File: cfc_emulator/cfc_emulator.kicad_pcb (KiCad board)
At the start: 2 copper layers, 51.3 x 51.1 mm, 23 parts, among them J1 pirt_test_conn, J2 PMOD1A, J3 PMOD1B, U1 DS90CR217MTD_NOPBMTD48_TEX-L

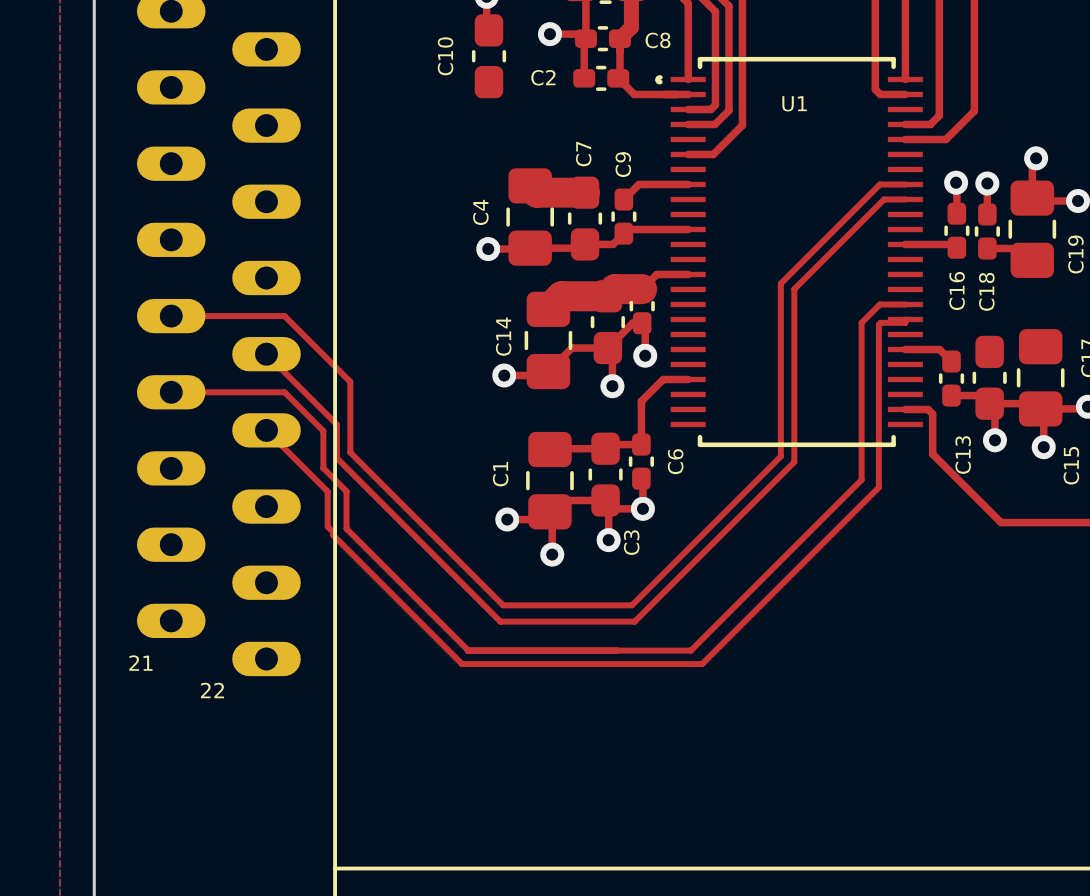
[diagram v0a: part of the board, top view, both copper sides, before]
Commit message: Tweak up diff pairs and remove gerbers
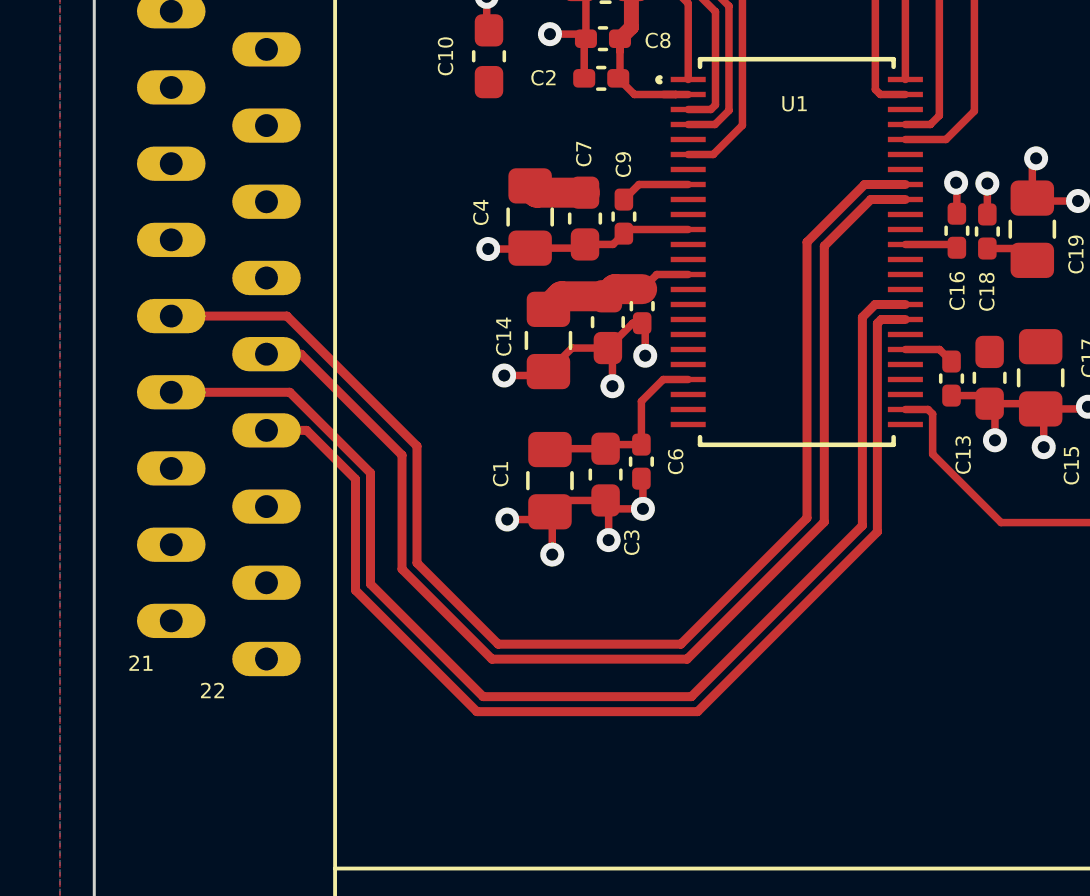
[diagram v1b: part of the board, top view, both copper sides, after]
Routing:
- net /LVDS0+: track 34.8 -> 39.5 mm
- net /LVDS0-: track 39.0 -> 43.0 mm
- net /LVDSCLK+: track 33.3 -> 36.8 mm
- net /LVDSCLK-: track 42.4 -> 40.3 mm
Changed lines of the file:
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@@
   (segment (start 163.137028 89.028528) (end 161.529613 89.028528) (width 0.25) (layer "F.Cu") (net 15))
   (segment (start 153.878528 84.028528) (end 153.456413 84.028528) (width 0.25) (layer "F.Cu") (net 15))
-  (segment (start 143.0274 95.9612) (end 148.122615 101.056415) (width 0.2) (layer "F.Cu") (net 21))
-  (segment (start 148.122615 101.056415) (end 152.415215 101.056415) (width 0.2) (layer "F.Cu") (net 21))
-  (segment (start 152.415215 101.056415) (end 157.3784 96.09323) (width 0.2) (layer "F.Cu") (net 21))
-  (segment (start 140.837418 91.4146) (end 143.0274 93.604582) (width 0.2) (layer "F.Cu") (net 21))
-  (segment (start 137.0584 91.4146) (end 140.837418 91.4146) (width 0.2) (layer "F.Cu") (net 21))
-  (segment (start 157.3784 96.09323) (end 157.3784 90.331817) (width 0.2) (layer "F.Cu") (net 21))
-  (segment (start 157.3784 90.331817) (end 160.681689 87.028528) (width 0.2) (layer "F.Cu") (net 21))
-  (segment (start 143.0274 93.604582) (end 143.0274 95.9612) (width 0.2) (layer "F.Cu") (net 21))
-  (segment (start 160.681689 87.028528) (end 161.529613 87.028528) (width 0.2) (layer "F.Cu") (net 21))
-  (segment (start 142.57789 95.02909) (end 142.57789 96.147394) (width 0.2) (layer "F.Cu") (net 22))
-  (segment (start 160.817393 87.528528) (end 161.529613 87.528528) (width 0.2) (layer "F.Cu") (net 22))
-  (segment (start 157.827911 96.279423) (end 157.827911 90.51801) (width 0.2) (layer "F.Cu") (net 22))
-  (segment (start 142.57789 96.147394) (end 148.030496 101.6) (width 0.2) (layer "F.Cu") (net 22))
-  (segment (start 140.2334 92.6846) (end 142.57789 95.02909) (width 0.2) (layer "F.Cu") (net 22))
-  (segment (start 152.507334 101.6) (end 157.827911 96.279423) (width 0.2) (layer "F.Cu") (net 22))
-  (segment (start 148.030496 101.6) (end 152.507334 101.6) (width 0.2) (layer "F.Cu") (net 22))
-  (segment (start 157.827911 90.51801) (end 160.817393 87.528528) (width 0.2) (layer "F.Cu") (net 22))
-  (segment (start 154.381364 102.565036) (end 160.0708 96.8756) (width 0.2) (layer "F.Cu") (net 23))
-  (segment (start 140.837418 93.9546) (end 142.128379 95.245561) (width 0.2) (layer "F.Cu") (net 23))
-  (segment (start 160.0708 96.8756) (end 160.0708 91.639417) (width 0.2) (layer "F.Cu") (net 23))
-  (segment (start 146.938836 102.565036) (end 151.942964 102.565036) (width 0.2) (layer "F.Cu") (net 23))
-  (segment (start 142.128379 96.483861) (end 142.900409 97.255891) (width 0.2) (layer "F.Cu") (net 23))
-  (segment (start 137.0584 93.9546) (end 140.837418 93.9546) (width 0.2) (layer "F.Cu") (net 23))
-  (segment (start 142.900409 97.255891) (end 142.900409 98.501209) (width 0.2) (layer "F.Cu") (net 23))
-  (segment (start 146.938836 102.539636) (end 146.938836 102.565036) (width 0.2) (layer "F.Cu") (net 23))
-  (segment (start 142.128379 95.245561) (end 142.128379 96.483861) (width 0.2) (layer "F.Cu") (net 23))
-  (segment (start 160.681689 91.028528) (end 161.529613 91.028528) (width 0.2) (layer "F.Cu") (net 23))
-  (segment (start 146.938836 102.565036) (end 154.381364 102.565036) (width 0.2) (layer "F.Cu") (net 23))
-  (segment (start 160.0708 91.639417) (end 160.681689 91.028528) (width 0.2) (layer "F.Cu") (net 23))
-  (segment (start 142.900409 98.501209) (end 146.938836 102.539636) (width 0.2) (layer "F.Cu") (net 23))
-  (segment (start 142.450889 98.712793) (end 142.450889 98.611193) (width 0.2) (layer "F.Cu") (net 24))
-  (segment (start 161.529613 91.528528) (end 161.529613 91.640117) (width 0.2) (layer "F.Cu") (net 24))
-  (segment (start 160.645902 91.700019) (end 160.645902 97.124459) (width 0.2) (layer "F.Cu") (net 24))
-  (segment (start 154.755816 103.014545) (end 146.752641 103.014545) (width 0.2) (layer "F.Cu") (net 24))
-  (segment (start 142.450889 98.611193) (end 142.273089 98.433393) (width 0.2) (layer "F.Cu") (net 24))
-  (segment (start 160.645902 97.124459) (end 154.755816 103.014545) (width 0.2) (layer "F.Cu") (net 24))
-  (segment (start 146.752641 103.014545) (end 142.450889 98.712793) (width 0.2) (layer "F.Cu") (net 24))
-  (segment (start 142.273089 98.433393) (end 142.273089 97.264289) (width 0.2) (layer "F.Cu") (net 24))
-  (segment (start 161.529613 91.640117) (end 160.705804 91.640117) (width 0.2) (layer "F.Cu") (net 24))
-  (segment (start 142.273089 97.264289) (end 140.2334 95.2246) (width 0.2) (layer "F.Cu") (net 24))
-  (segment (start 160.705804 91.640117) (end 160.645902 91.700019) (width 0.2) (layer "F.Cu") (net 24))
+  (segment (start 137.0584 91.4146) (end 140.9146 91.4146) (width 0.3) (layer "F.Cu") (net 21))
+  (segment (start 154.045957 102.350489) (end 158.250489 98.145957) (width 0.3) (layer "F.Cu") (net 21))
+  (segment (start 140.9146 91.4146) (end 145.25 95.75) (width 0.3) (layer "F.Cu") (net 21))
+  (segment (start 158.250489 88.949511) (end 160.171472 87.028528) (width 0.3) (layer "F.Cu") (net 21))
+  (segment (start 145.25 99.643584) (end 147.956905 102.350489) (width 0.3) (layer "F.Cu") (net 21))
+  (segment (start 158.250489 98.145957) (end 158.250489 88.949511) (width 0.3) (layer "F.Cu") (net 21))
+  (segment (start 147.956905 102.350489) (end 154.045957 102.350489) (width 0.3) (layer "F.Cu") (net 21))
+  (segment (start 160.171472 87.028528) (end 161.529613 87.028528) (width 0.3) (layer "F.Cu") (net 21))
+  (segment (start 145.25 95.75) (end 145.25 99.643584) (width 0.3) (layer "F.Cu") (net 21))
+  (segment (start 144.750489 99.850489) (end 147.75 102.85) (width 0.3) (layer "F.Cu") (net 22))
+  (segment (start 160.377888 87.528528) (end 161.529613 87.528528) (width 0.3) (layer "F.Cu") (net 22))
+  (segment (start 147.75 102.85) (end 154.253554 102.85) (width 0.3) (layer "F.Cu") (net 22))
+  (segment (start 144.750489 96.050489) (end 144.750489 99.850489) (width 0.3) (layer "F.Cu") (net 22))
+  (segment (start 140.2334 92.6846) (end 141.3846 92.6846) (width 0.3) (layer "F.Cu") (net 22))
+  (segment (start 158.826777 89.079639) (end 160.377888 87.528528) (width 0.3) (layer "F.Cu") (net 22))
+  (segment (start 158.826777 98.276777) (end 158.826777 89.079639) (width 0.3) (layer "F.Cu") (net 22))
+  (segment (start 141.3846 92.6846) (end 144.750489 96.050489) (width 0.3) (layer "F.Cu") (net 22))
+  (segment (start 154.253554 102.85) (end 158.826777 98.276777) (width 0.3) (layer "F.Cu") (net 22))
+  (segment (start 141.011015 93.9546) (end 143.7 96.643585) (width 0.3) (layer "F.Cu") (net 23))
+  (segment (start 160.520299 91.028528) (end 161.529613 91.028528) (width 0.3) (layer "F.Cu") (net 23))
+  (segment (start 143.7 100.346446) (end 147.453554 104.1) (width 0.3) (layer "F.Cu") (net 23))
+  (segment (start 143.7 96.643585) (end 143.7 100.346446) (width 0.3) (layer "F.Cu") (net 23))
+  (segment (start 160.095911 98.400535) (end 160.095911 91.452916) (width 0.3) (layer "F.Cu") (net 23))
+  (segment (start 137.0584 93.9546) (end 141.011015 93.9546) (width 0.3) (layer "F.Cu") (net 23))
+  (segment (start 160.095911 91.452916) (end 160.520299 91.028528) (width 0.3) (layer "F.Cu") (net 23))
+  (segment (start 147.453554 104.1) (end 154.396446 104.1) (width 0.3) (layer "F.Cu") (net 23))
+  (segment (start 154.396446 104.1) (end 160.095911 98.400535) (width 0.3) (layer "F.Cu") (net 23))
+  (segment (start 141.5746 95.2246) (end 143.2 96.85) (width 0.3) (layer "F.Cu") (net 24))
+  (segment (start 154.603554 104.6) (end 160.595902 98.607652) (width 0.3) (layer "F.Cu") (net 24))
+  (segment (start 143.2 96.85) (end 143.2 100.553554) (width 0.3) (layer "F.Cu") (net 24))
+  (segment (start 160.595902 91.660019) (end 160.727393 91.528528) (width 0.3) (layer "F.Cu") (net 24))
+  (segment (start 147.246446 104.6) (end 154.603554 104.6) (width 0.3) (layer "F.Cu") (net 24))
+  (segment (start 160.727393 91.528528) (end 161.529613 91.528528) (width 0.3) (layer "F.Cu") (net 24))
+  (segment (start 160.595902 98.607652) (end 160.595902 91.660019) (width 0.3) (layer "F.Cu") (net 24))
+  (segment (start 140.2334 95.2246) (end 141.5746 95.2246) (width 0.3) (layer "F.Cu") (net 24))
+  (segment (start 143.2 100.553554) (end 147.246446 104.6) (width 0.3) (layer "F.Cu") (net 24))
   (segment (start 170.2816 74.7776) (end 175.26 79.756) (width 0.25) (layer "F.Cu") (net 25))
   (segment (start 170.2816 73.9836) (end 170.2816 74.7776) (width 0.25) (layer "F.Cu") (net 25))

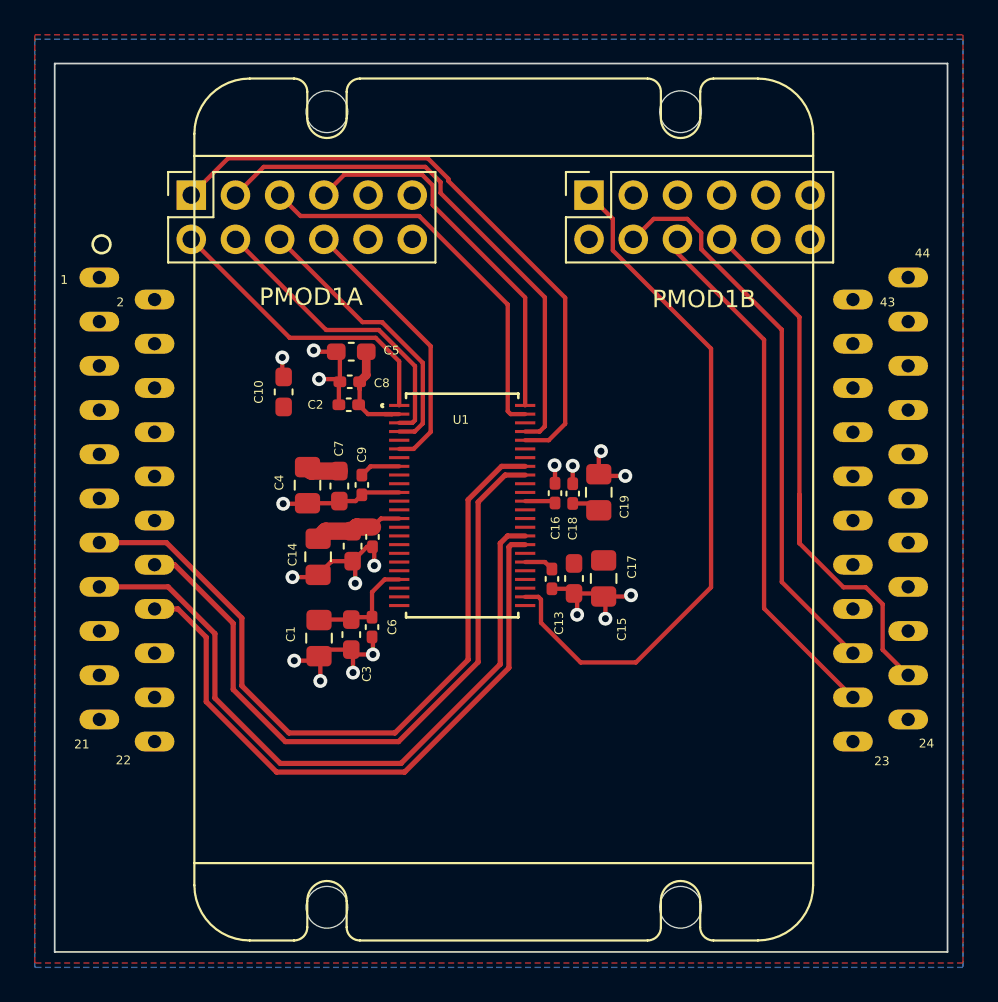
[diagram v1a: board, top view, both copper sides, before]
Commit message: Fix ~powerdown handling to add GPIO control from Icebreaker.  Add pullup on ~powerdown to default it to powered up.  Fix footprint error on TX chip (two pins swapped).  Fix pin swap error on both LVDS pairs.  Add test points to ~powerdown and TXCLK
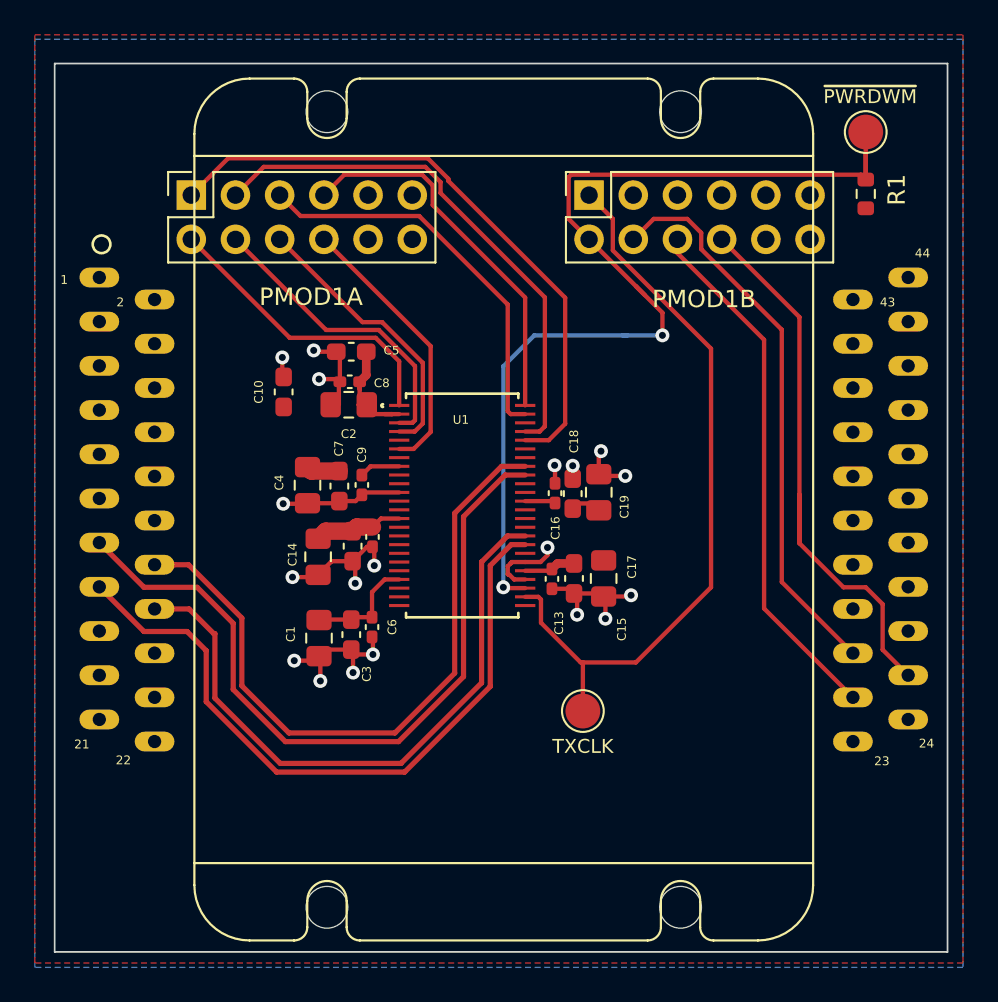
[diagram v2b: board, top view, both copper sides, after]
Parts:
- added R1: 10K, Resistor_SMD:R_0603_1608Metric, F.Cu at (181.1, 71.4)
- added TP1: TXCLK, TestPoint:TestPoint_Pad_D2.0mm, F.Cu at (164.8, 101.1)
- added TP2: ~POWERDOWN, TestPoint:TestPoint_Pad_D2.0mm, F.Cu at (181.1, 67.8)
- C18: footprint Capacitor_SMD:C_0402_1005Metric_Pad0.74x0.62mm_HandSolder -> Capacitor_SMD:C_0603_1608Metric_Pad1.08x0.95mm_HandSolder
- C2: footprint Capacitor_SMD:C_0402_1005Metric_Pad0.74x0.62mm_HandSolder -> Capacitor_SMD:C_0805_2012Metric_Pad1.18x1.45mm_HandSolder
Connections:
- J1 pad 13: /LVDS0- -> /LVDS0+
- J1 pad 14: /LVDS0+ -> /LVDS0-
- J1 pad 15: /LVDSCLK- -> /LVDSCLK+
- J1 pad 16: /LVDSCLK+ -> /LVDSCLK-
- J3 pad 7: unconnected-(J3-Pad7) -> /~PWRDOWN
- U1 pad 27: unconnected-(U1-Pad27) -> /~PWRDOWN
- U1 pad 28: (no net) -> GND
- U1 pad 29: (no net) -> +3V3
- U1 pad 30: +3V3 -> GND
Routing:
- net /~PWRDOWN: track 0.00 -> 57.6 mm, vias 0 -> 2
- net GND: track 42.8 -> 47.4 mm, vias 18 -> 19
- net /LVDS0+: track 39.5 -> 43.2 mm
- net /LVDSCLK+: track 36.8 -> 40.1 mm
- net /LVDSCLK-: track 40.3 -> 37.2 mm
- net /TXCLK: track 40.3 -> 43.0 mm
- net /LVDS0-: track 43.0 -> 40.5 mm
- net +3V3: track 27.6 -> 28.9 mm
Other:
- board text added: "TXCLK"
- board text added: "~PWRDWM"
